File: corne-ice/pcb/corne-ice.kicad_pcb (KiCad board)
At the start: 2 copper layers, 274.3 x 91.5 mm, 97 parts, among them J3 BAT, J4 nice!view, SW1 SW_PUSH, SW10 SW_PUSH, SW11 SW_PUSH, SW12 SW_PUSH, SW13 SW_PUSH, SW14 SW_PUSH, SW15 SW_PUSH, SW16 SW_PUSH, SW17 SW_PUSH, SW18 SW_PUSH, SW19 SW_PUSH, SW2 SW_PUSH, SW20 SW_PUSH, SW21 SW_PUSH, SW22 SW_PUSH, SW23 SW_PUSH, SW24 SW_PUSH, SW25 SW_PUSH, SW26 SW_PUSH, SW27 SW_PUSH, SW28 SW_PUSH, SW29 SW_PUSH, SW3 SW_PUSH, SW30 SW_PUSH, SW31 SW_PUSH, SW32 SW_PUSH, SW33 SW_PUSH, SW34 SW_PUSH, SW35 SW_PUSH, SW36 SW_PUSH, SW37 SW_PUSH, SW38 SW_PUSH, SW39 SW_PUSH, SW4 SW_PUSH, SW40 SW_PUSH, SW41 SW_PUSH, SW42 SW_PUSH, SW43 RotaryEncoder_Switch, SW44 SW_PUSH, SW5 SW_PUSH, SW6 SW_PUSH, SW7 SW_PUSH, SW8 SW_PUSH, SW9 SW_PUSH, U1 nice!nano, U2 nice!nano

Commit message: Left part updated
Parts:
- removed D10, D11, D12, D13, D14, D15, D16, D17, D18, D19, D20, D21, D43, D7, D8, D9: D, kbd:D3_SMD_v2
- removed the D4 at (84.7, 28.7)
- removed SW10, SW11, SW12, SW13, SW14, SW15, SW16, SW17, SW18, SW19, SW20, SW44, SW6, SW7, SW8, SW9: SW_PUSH, kbd:CherryMX_Hotswap
- removed SW21: SW_PUSH, kbd:CherryMX_Hotswap_1.5u
- removed the SW4 at (77.1, 28.7)
- added D4 (x2): D, kbd:D3_SMD_v2, B.Cu at (114.9, 93.1)
- added D44: D, kbd:D3_SMD_v2, B.Cu at (28.0, 54.8)
- added D45: D, kbd:D3_SMD_v2, B.Cu at (28.0, 73.8)
- added D46: D, kbd:D3_SMD_v2, B.Cu at (47.0, 35.8)
- added D47: D, kbd:D3_SMD_v2, B.Cu at (47.0, 54.8)
- added D48: D, kbd:D3_SMD_v2, B.Cu at (47.0, 73.8)
- added D49: D, kbd:D3_SMD_v2, B.Cu at (66.0, 31.0)
- added D50: D, kbd:D3_SMD_v2, B.Cu at (66.0, 50.0)
- added D51: D, kbd:D3_SMD_v2, B.Cu at (66.0, 69.0)
- added D52: D, kbd:D3_SMD_v2, B.Cu at (85.0, 28.8)
- added D53: D, kbd:D3_SMD_v2, B.Cu at (85.0, 47.8)
- added D54: D, kbd:D3_SMD_v2, B.Cu at (85.0, 66.8)
- added D55: D, kbd:D3_SMD_v2, B.Cu at (104.0, 31.0)
- added D56: D, kbd:D3_SMD_v2, B.Cu at (104.0, 50.0)
- added D57: D, kbd:D3_SMD_v2, B.Cu at (104.0, 69.0)
- added D58: D, kbd:D3_SMD_v2, B.Cu at (123.0, 33.2)
- added D59: D, kbd:D3_SMD_v2, B.Cu at (123.0, 52.2)
- added D60: D, kbd:D3_SMD_v2, B.Cu at (123.0, 71.2)
- added SW4 (x2): SW_PUSH, kbd:CherryMX_Hotswap, F.Cu at (107.2, 91.0)
- added SW45: SW_PUSH, kbd:CherryMX_Hotswap, F.Cu at (20.0, 54.8)
- added SW46: SW_PUSH, kbd:CherryMX_Hotswap, F.Cu at (20.0, 73.8)
- added SW47: SW_PUSH, kbd:CherryMX_Hotswap, F.Cu at (39.0, 35.8)
- added SW48: SW_PUSH, kbd:CherryMX_Hotswap, F.Cu at (39.0, 54.8)
- added SW49: SW_PUSH, kbd:CherryMX_Hotswap, F.Cu at (39.0, 73.8)
- added SW50: SW_PUSH, kbd:CherryMX_Hotswap, F.Cu at (58.0, 31.0)
- added SW51: SW_PUSH, kbd:CherryMX_Hotswap, F.Cu at (58.0, 50.0)
- added SW52: SW_PUSH, kbd:CherryMX_Hotswap, F.Cu at (58.0, 69.0)
- added SW53: SW_PUSH, kbd:CherryMX_Hotswap, F.Cu at (77.0, 28.8)
- added SW54: SW_PUSH, kbd:CherryMX_Hotswap, F.Cu at (77.0, 47.8)
- added SW55: SW_PUSH, kbd:CherryMX_Hotswap, F.Cu at (77.0, 66.8)
- added SW56: SW_PUSH, kbd:CherryMX_Hotswap, F.Cu at (96.0, 31.0)
- added SW57: SW_PUSH, kbd:CherryMX_Hotswap, F.Cu at (96.0, 50.0)
- added SW58: SW_PUSH, kbd:CherryMX_Hotswap, F.Cu at (96.0, 69.0)
- added SW59: SW_PUSH, kbd:CherryMX_Hotswap, F.Cu at (115.0, 33.2)
- added SW60: SW_PUSH, kbd:CherryMX_Hotswap, F.Cu at (115.0, 52.2)
- added SW61: SW_PUSH, kbd:CherryMX_Hotswap, F.Cu at (115.0, 71.2)
- SW5: footprint kbd:CherryMX_Hotswap -> kbd:CherryMX_Hotswap_1.5u
- moved SW5 72.1 mm to (129.4, 95.0), turned to 60 degrees
- moved D5 64.3 mm to (133.4, 88.1), turned to 150 degrees
- moved D3 64.0 mm to (94.0, 88.2)
- moved SW3 63.6 mm to (86.0, 88.2)
- moved D2 59.6 mm to (75.0, 88.2)
- moved SW2 59.4 mm to (67.0, 88.2)
- moved D6 41.0 mm to (138.7, 71.2)
- moved SW43 0.42 mm to (126.8, 68.5)
- moved PSW1 0.32 mm to (143.0, 81.0)
- moved D1 0.27 mm to (28.0, 35.8)
- moved RSW1 0.25 mm to (143.0, 64.0)
- moved SW1 0.11 mm to (20.0, 35.8)
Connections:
- D2 pad 1: row0 -> row3
- D3 pad 1: row0 -> row3
- D5 pad 1: row0 -> row3
- D6 pad 1: row0 -> row3
- SW2 pad 1: col1 -> col2
- SW3 pad 1: col2 -> col3
- SW43 pad A: unconnected-(SW43-PadA) -> rotary_a
- SW43 pad B: unconnected-(SW43-PadB) -> rotary_b
- SW43 pad C: unconnected-(SW43-PadC) -> GND
- SW43 pad S1: unconnected-(SW43-PadS1) -> col1
- SW43 pad S2: unconnected-(SW43-PadS2) -> Net-(D6-A)
- SW5 pad 1: col4 -> col5
- U1 pad 13: unconnected-(U1-NFC1/P0.09-Pad13) -> rotary_a
- U1 pad 14: unconnected-(U1-NFC2/P0.10-Pad14) -> rotary_b
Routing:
- net GNDA: track 78.2 -> 26.2 mm
- net col1: track 153.5 -> 185.6 mm
- net reset_r: track 73.0 -> 50.8 mm
- net rotary_b: track 0.00 -> 17.4 mm
- net GND: track 56.1 -> 73.4 mm, vias 2 -> 0
- net col0: track 172.6 -> 158.2 mm
- net col5_r: track 86.4 -> 73.9 mm
- net rotary_a: track 0.00 -> 9.52 mm
- net col2: track 155.6 -> 146.5 mm
- net col3: track 137.2 -> 129.3 mm
- net Net-(J3-Pin_1): track 68.8 -> 60.9 mm
- net Net-(D21-A): track 7.81 -> 0.00 mm
- net Net-(D43-A): track 4.62 -> 0.00 mm
- net col0_r: track 175.8 -> 171.3 mm
- net RAW: track 58.7 -> 63.1 mm, vias 1 -> 0
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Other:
- board size 274.3 x 91.5 mm -> 274.7 x 92.1 mm
- board text removed: "- GND"

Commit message: Right half
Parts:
- removed the D4 at (114.9, 93.1)
- removed J3: BAT, Connector_JST:JST_PH_S2B-PH-SM4-TB_1x02-1MP_P2.00mm_Horizontal
- removed J4: nice!view, Connector_PinHeader_2.54mm:PinHeader_1x05_P2.54mm_Vertical
- removed RSW2: SW_PUSH, keeblib:alps_sksn
- removed the SW4 at (107.2, 91.0)
- added D7: D, kbd:D3_SMD_v2, B.Cu at (238.0, 88.2)
- added D8: D, kbd:D3_SMD_v2, B.Cu at (157.6, 71.0)
- added RSW3: SW_PUSH, Button_Switch_SMD:SW_Push_1P1T-MP_NO_Horizontal_Alps_SKRTLAE010, F.Cu at (154.1, 64.0)
- added SW6: SW_PUSH, kbd:CherryMX_Hotswap, F.Cu at (230.0, 88.2)
- added SW7: RotaryEncoder_Switch, Rotary_Encoder:RotaryEncoder_Alps_EC11E-Switch_Vertical_H20mm, F.Cu at (169.5, 73.5)
- added TP3: TestPoint, TestPoint:TestPoint_Pad_D1.5mm, F.Cu at (169.6, 63.5)
- added TP4: TestPoint, TestPoint:TestPoint_Pad_1.5x1.5mm, F.Cu at (166.0, 63.5)
- PSW2: moved to F.Cu
- moved PSW2 52.9 mm to (154.0, 81.0), turned to -90 degrees
- moved D42 28.7 mm to (171.4, 101.9), turned to 30 degrees
- moved D41 2.14 mm to (197.5, 88.8), turned to 105 degrees
- moved D40 1.36 mm to (219.0, 88.2)
- moved SW40 0.99 mm to (211.0, 88.2)
- moved D27 0.82 mm to (190.0, 33.2)
- moved D33 0.82 mm to (190.0, 52.2)
- moved D39 0.82 mm to (190.0, 71.2)
- moved D28 0.80 mm to (285.0, 54.8)
- moved D25 0.80 mm to (228.0, 28.8)
- moved D31 0.80 mm to (228.0, 47.8)
- moved D37 0.80 mm to (228.0, 66.8)
- moved SW41 0.79 mm to (189.8, 91.0)
- moved D36 0.79 mm to (247.0, 69.0)
- moved D38 0.79 mm to (209.0, 69.0)
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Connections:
- U2 pad 13: unconnected-(U2-NFC1/P0.09-Pad13) -> rotary_a_r
- U2 pad 14: unconnected-(U2-NFC2/P0.10-Pad14) -> rotary_b_r
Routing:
- net row0_r: track 180.3 -> 130.8 mm, vias 2 -> 0
- net GNDA: track 26.2 -> 75.6 mm
- net RAW_r: track 1.53 -> 50.2 mm, vias 0 -> 1
- net row3_r: track 94.7 -> 140.9 mm, vias 2 -> 0
- net row1_r: track 166.2 -> 124.0 mm
- net row2_r: track 172.0 -> 133.4 mm, vias 2 -> 0
- net CS_r: track 37.1 -> 0.00 mm
- net rotary_a_r: track 0.00 -> 34.0 mm
- net MOSI_r: track 33.6 -> 0.00 mm
- net Net-(D42-A): track 33.7 -> 4.20 mm
- net SCK_r: track 28.9 -> 0.00 mm
- net VDD: track 28.4 -> 0.00 mm, vias 1 -> 0
- net Net-(PSW2-B): track 60.9 -> 32.6 mm, vias 1 -> 0
- net col2_r: track 124.8 -> 147.2 mm
- net rotary_b_r: track 0.00 -> 21.8 mm
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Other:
- board size 274.7 x 92.1 mm -> 275.5 x 92.1 mm
- board text added: "+VCC"
- board text added: "-GND"
- board text added: "GND-"
- board text added: "VCC+"
- board text removed: "+ VCC"
- board text removed: "GND -"
- board text removed: "VCC +"

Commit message: Smoothed outline and added holes.
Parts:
- added REF**: M2_Hole_NPTH_Outside, kbd:M2_Hole_NPTH_Outside, F.Cu at (220.5, 78.7)
- added REF**: M2_Hole_NPTH_Outside, kbd:M2_Hole_NPTH_Outside, B.Cu at (29.5, 45.3)
- added REF**: M2_Hole_NPTH_Outside, kbd:M2_Hole_NPTH_Outside, F.Cu at (267.5, 64.3)
- added REF**: M2_Hole_NPTH_Outside, kbd:M2_Hole_NPTH_Outside, F.Cu at (178.1, 84.4)
- added REF**: M2_Hole_NPTH_Outside, kbd:M2_Hole_NPTH_Outside, F.Cu at (191.5, 40.5)
- added REF**: M2_Hole_NPTH_Outside, kbd:M2_Hole_NPTH_Outside, F.Cu at (267.5, 45.3)
- added REF**: M2_Hole_NPTH_Outside, kbd:M2_Hole_NPTH_Outside, B.Cu at (29.5, 64.3)
- added REF**: M2_Hole_NPTH_Outside, kbd:M2_Hole_NPTH_Outside, B.Cu at (105.5, 40.5)
- added REF**: M2_Hole_NPTH_Outside, kbd:M2_Hole_NPTH_Outside, B.Cu at (118.9, 84.4)
- added REF**: M2_Hole_NPTH_Outside, kbd:M2_Hole_NPTH_Outside, B.Cu at (76.5, 78.7)
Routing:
- net col0_r: track 160.8 -> 163.4 mm
- net col3_r: track 129.8 -> 132.5 mm
- net col2_r: track 147.2 -> 149.8 mm
- net col1_r: track 168.4 -> 171.1 mm
- net col2: track 146.5 -> 148.5 mm
- net col3: track 129.3 -> 131.3 mm
- net col1: track 185.7 -> 187.6 mm
- net col0: track 157.3 -> 159.0 mm
- net row0_r: track 130.8 -> 129.9 mm
- net row2_r: track 133.4 -> 132.6 mm
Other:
- outline, holes or cut-outs redrawn

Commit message: Backup.
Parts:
- added REF**: Breakaway_Tabs, kbd:Breakaway_Tabs, B.Cu at (230.1, 97.7)
- added REF**: Breakaway_Tabs, kbd:Breakaway_Tabs, B.Cu at (276.9, 83.2)
- added REF**: Breakaway_Tabs, kbd:Breakaway_Tabs, B.Cu at (238.9, 21.5)
- added REF**: Breakaway_Tabs, kbd:Breakaway_Tabs, B.Cu at (200.8, 21.5)
- added REF**: Breakaway_Tabs, kbd:Breakaway_Tabs, F.Cu at (96.1, 21.5)
- added REF**: Breakaway_Tabs, kbd:Breakaway_Tabs, F.Cu at (20.0, 83.2)
- added REF**: Breakaway_Tabs, kbd:Breakaway_Tabs, F.Cu at (58.0, 21.5)
- added REF**: Breakaway_Tabs, kbd:Breakaway_Tabs, F.Cu at (66.9, 97.7)
- D1, D2, D22, D23, D24, D25, D26, D27, D28, D29, D3, D30, D31, D32, D33, D34, D35, D36, D37, D38, D39, D4, D40, D41, D42, D44, D45, D46, D47, D48, D49, D5, D50, D51, D52, D53, D54, D55, D56, D57, D58, D59, D6, D60, D7, D8: footprint kbd:D3_SMD_v2 -> Diode_SMD:D_SOD-123
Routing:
- net col3_r: vias 5 -> 4
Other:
- board size 275.5 x 92.1 mm -> 275.4 x 100 mm
- board text removed: "Corne-ice v0.1 PCB Designed by foostan/e3b0c442"

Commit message: Ordered.
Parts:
- removed the REF** at (220.5, 78.7)
- removed the REF** at (29.5, 64.3)
- removed the REF** at (105.5, 40.5)
- removed the REF** at (118.9, 84.4)
- removed the REF** at (76.5, 78.7)
- removed the REF** at (29.5, 45.3)
- removed the REF** at (267.5, 64.3)
- removed the REF** at (178.1, 84.4)
- removed the REF** at (191.5, 40.5)
- removed the REF** at (267.5, 45.3)
- added REF**: M2_Hole_NPTH_Outside, kbd:M2_Hole_NPTH_Outside, B.Cu at (38.5, 47.5)
- added REF**: M2_Hole_NPTH_Outside, kbd:M2_Hole_NPTH_Outside, B.Cu at (38.5, 66.5)
- added REF**: M2_Hole_NPTH_Outside, kbd:M2_Hole_NPTH_Outside, B.Cu at (85.5, 80.9)
- added REF**: M2_Hole_NPTH_Outside, kbd:M2_Hole_NPTH_Outside, B.Cu at (130.5, 85.5)
- added REF**: M2_Hole_NPTH_Outside, kbd:M2_Hole_NPTH_Outside, B.Cu at (114.5, 43.5)
- added REF**: M2_Hole_NPTH_Outside, kbd:M2_Hole_NPTH_Outside, F.Cu at (184.5, 85.5)
- added REF**: M2_Hole_NPTH_Outside, kbd:M2_Hole_NPTH_Outside, F.Cu at (200.5, 43.5)
- added REF**: M2_Hole_NPTH_Outside, kbd:M2_Hole_NPTH_Outside, F.Cu at (276.5, 66.5)
- added REF**: M2_Hole_NPTH_Outside, kbd:M2_Hole_NPTH_Outside, F.Cu at (276.5, 47.5)
- added REF**: M2_Hole_NPTH_Outside, kbd:M2_Hole_NPTH_Outside, F.Cu at (229.5, 80.9)
- RSW1, SW1, SW2, SW22, SW23, SW24, SW25, SW26, SW27, SW28, SW29, SW3, SW30, SW31, SW32, SW33, SW34, SW35, SW36, SW37, SW38, SW39, SW4, SW40, SW41, SW42, SW45, SW46, SW47, SW48, SW49, SW5, SW50, SW51, SW52, SW53, SW54, SW55, SW56, SW57, SW58, SW59, SW6, SW60, SW61: value SW_PUSH -> CPG151101S11-16
- RSW2: renamed from RSW3; value SW_PUSH -> CPG151101S11-16
- moved SW43 9.26 mm to (135.8, 70.7)
- moved TP1 9.26 mm to (139.6, 65.7)
- moved TP2 9.26 mm to (136.3, 65.7)
- moved D1 9.26 mm to (37.0, 38.0)
- moved D2 9.26 mm to (84.0, 90.4)
- moved D22 9.26 mm to (294.0, 38.0)
- moved D23 9.26 mm to (275.0, 38.0)
- moved D24 9.26 mm to (256.0, 33.2)
- moved D25 9.26 mm to (237.0, 31.0)
- moved D26 9.26 mm to (218.0, 33.2)
- moved D28 9.26 mm to (294.0, 57.0)
- moved D29 9.26 mm to (275.0, 57.0)
- moved D3 9.26 mm to (103.0, 90.4)
- moved D30 9.26 mm to (256.0, 52.2)
- moved D31 9.26 mm to (237.0, 50.0)
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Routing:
- net GNDA: track 75.6 -> 74.9 mm
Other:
- outline, holes or cut-outs redrawn

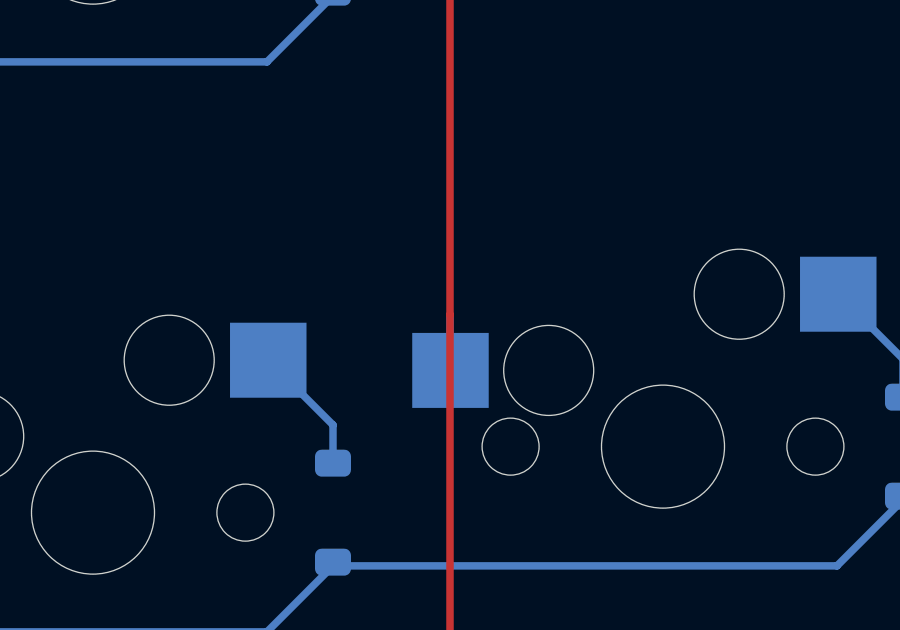
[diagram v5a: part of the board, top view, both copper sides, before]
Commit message: Fixes missing via.
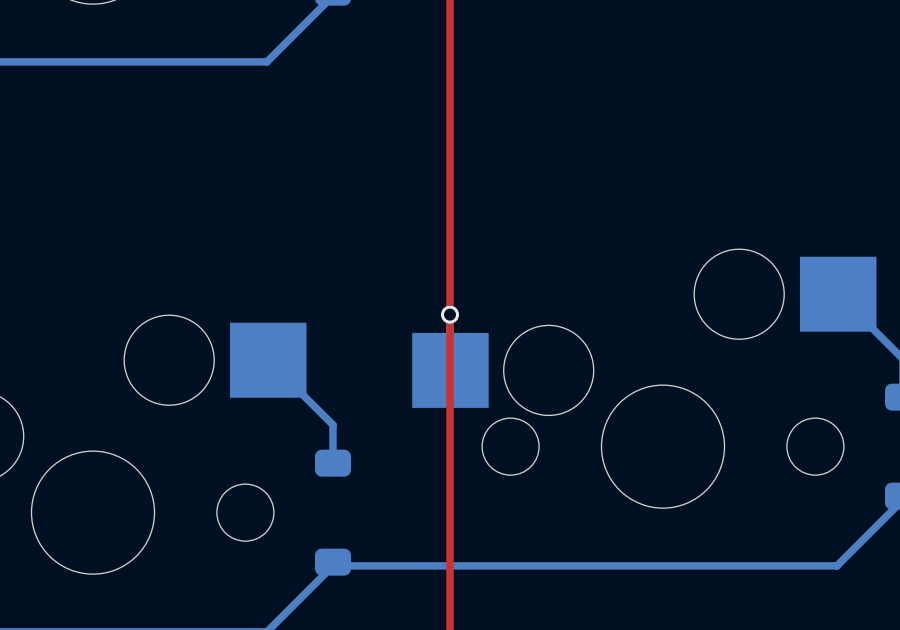
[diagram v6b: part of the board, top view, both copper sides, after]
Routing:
- net col3_r: track 132.5 -> 132.7 mm, vias 4 -> 5
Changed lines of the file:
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@@
   (segment (start 221.9 30.4) (end 221.9 64.6) (width 0.25) (layer "F.Cu") (net 21))
   (segment (start 179.645373 50.6) (end 164.6934 50.6) (width 0.25) (layer "F.Cu") (net 21))
+  (segment (start 221.9 64.6) (end 221.9 64.8) (width 0.25) (layer "F.Cu") (net 21))
   (segment (start 221.9 64.6) (end 221.9 77) (width 0.25) (layer "F.Cu") (net 21))
   (segment (start 182.7 47.545373) (end 179.645373 50.6) (width 0.25) (layer "F.Cu") (net 21))
@@
   (via (at 182.7 47.545373) (size 0.6) (drill 0.4) (layers "F.Cu" "B.Cu") (net 21))
   (via (at 221.9 30.4) (size 0.6) (drill 0.4) (layers "F.Cu" "B.Cu") (net 21))
+  (via (at 221.9 64.6) (size 0.6) (drill 0.4) (layers "F.Cu" "B.Cu") (net 21))
   (via (at 212.9 86) (size 0.6) (drill 0.4) (layers "F.Cu" "B.Cu") (net 21))
   (via (at 221.915 45.515) (size 0.6) (drill 0.4) (layers "F.Cu" "B.Cu") (net 21))
